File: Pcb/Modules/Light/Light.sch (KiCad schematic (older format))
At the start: 20 parts, among them J1 JACK_RJ45, J2 JACK_STEREO, Q1 TEPT4400, Q2 Q_NMOS_GSD, U1 74LVC1G07, U2 74LVC1G07

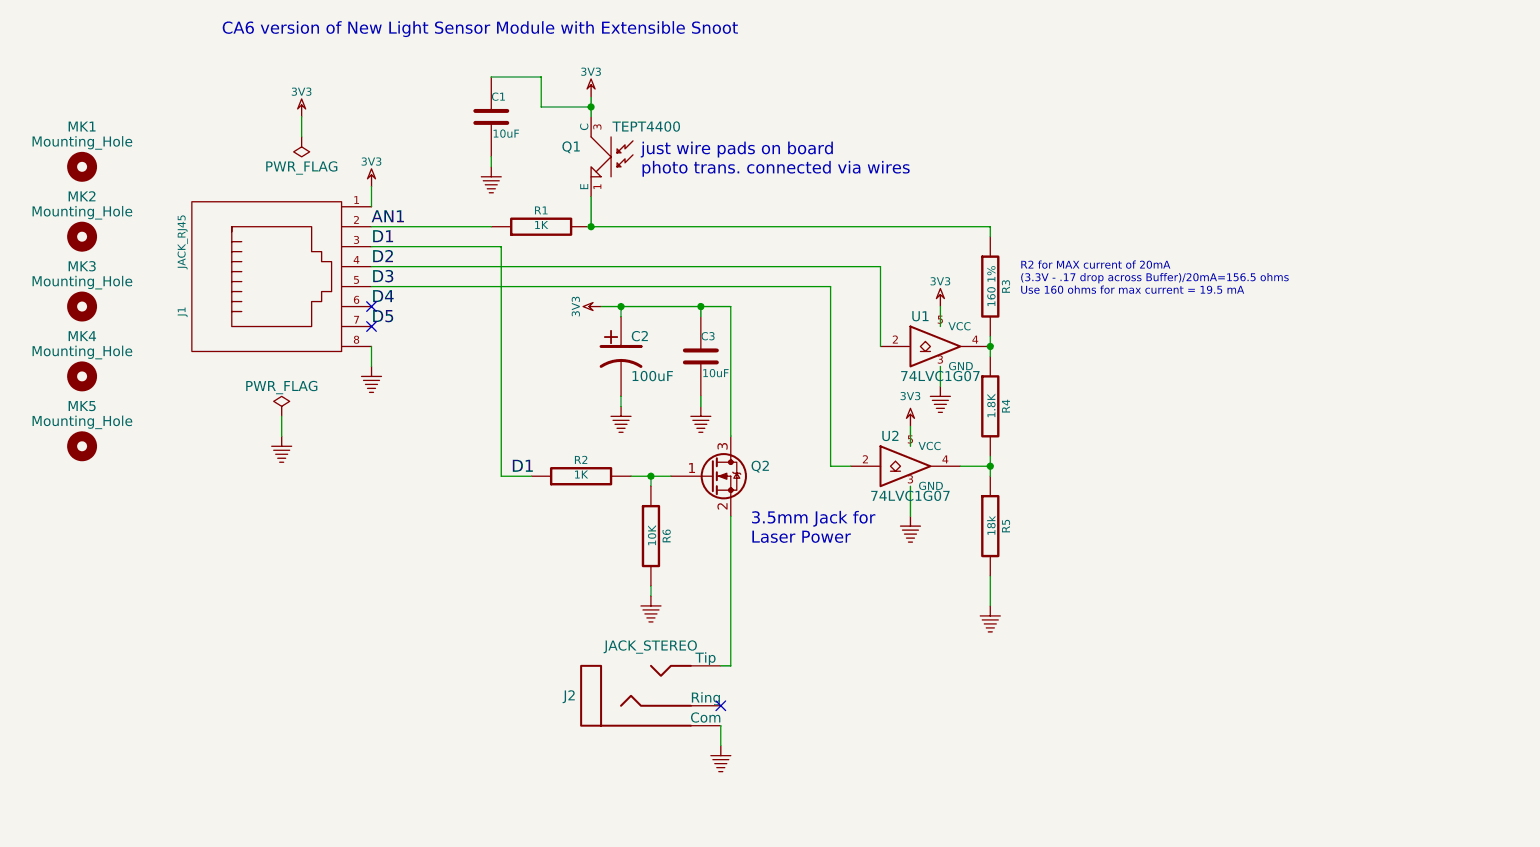
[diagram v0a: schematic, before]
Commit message: Updated schematic for 4-resistor ladder with good values, and moved MOSFET to low (working) position.  PCB only partially updated.  Used a 3rd single buffer for now because I didn't see an exact equivalent in a quad buffer, but that is a likely option.
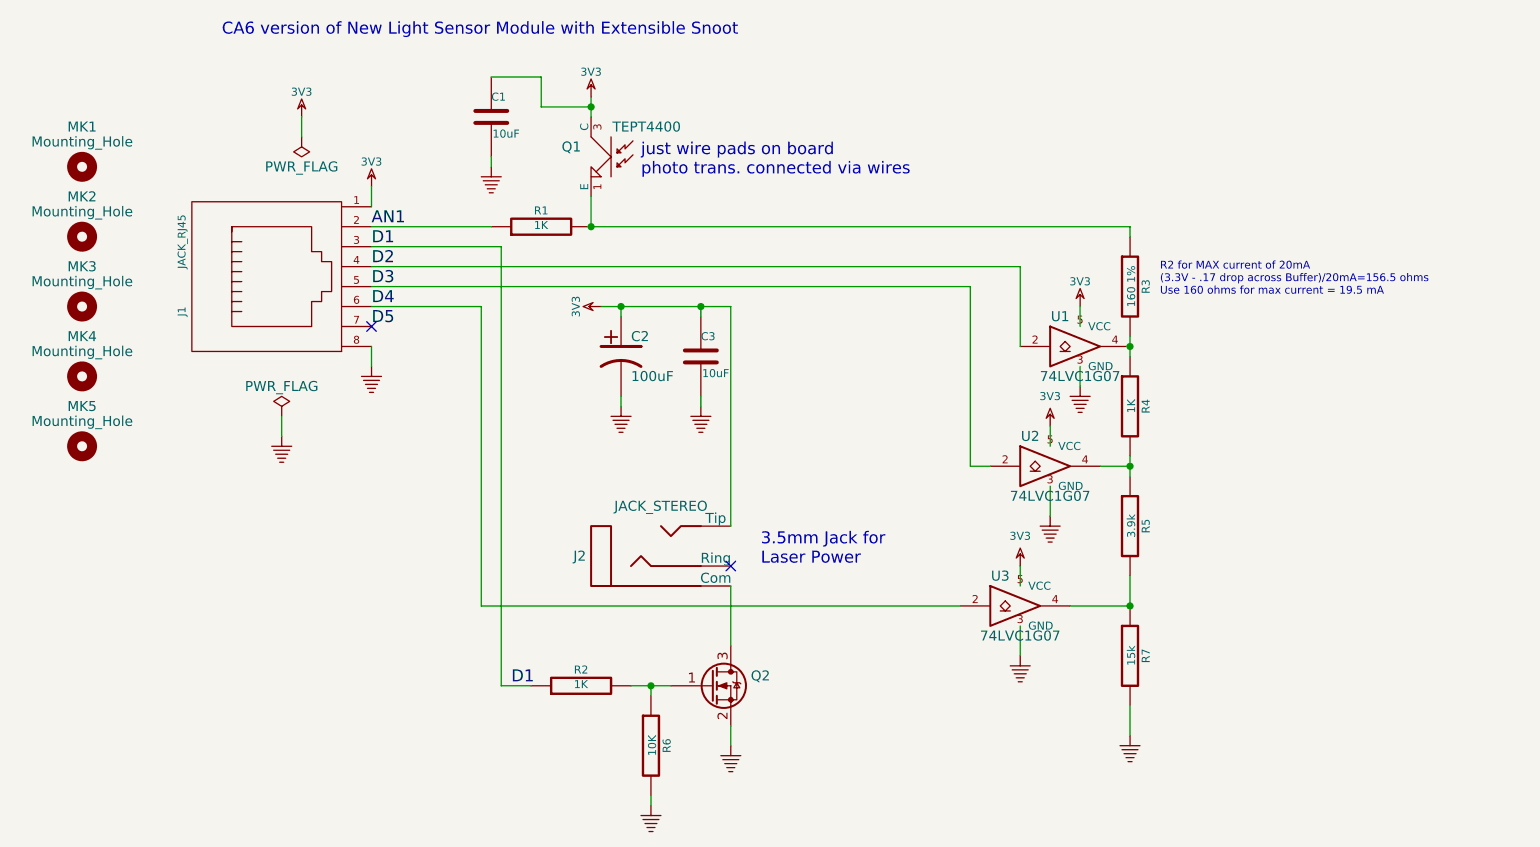
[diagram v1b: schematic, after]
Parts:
- added R7: 15k, CA6:SM0603_Resistor, symbol R
- added U3: 74LVC1G07, TO_SOT_Packages_SMD:SOT-353_SC-70-5, symbol 74LVC1G07
- R4: value 1.8K -> 1K
- R5: value 18k -> 3.9k
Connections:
- net 3V3: now also J2.2 (Tip), U3.5 (VCC); no longer Q2.3 (D)
- net D4: now also U3.2
- net GND: now also Q2.2 (S), R7.2, U3.3 (GND); no longer J2.3 (Com), R5.2
- new net: J2.3 (Com), Q2.3 (D)
- new net: R5.2, R7.1, U3.4
- no-connect marks 3 -> 2
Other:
- moved on the sheet: J2, Q2, R2, R3, R4, R5, R6, U1, U2

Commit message: Updated light module for 3rd buffer and 4 resistors in the ladder, and updated resistor values to give a good change at each step.  Todo: incorporate auto-sensitivity changes into Lightning Menu.
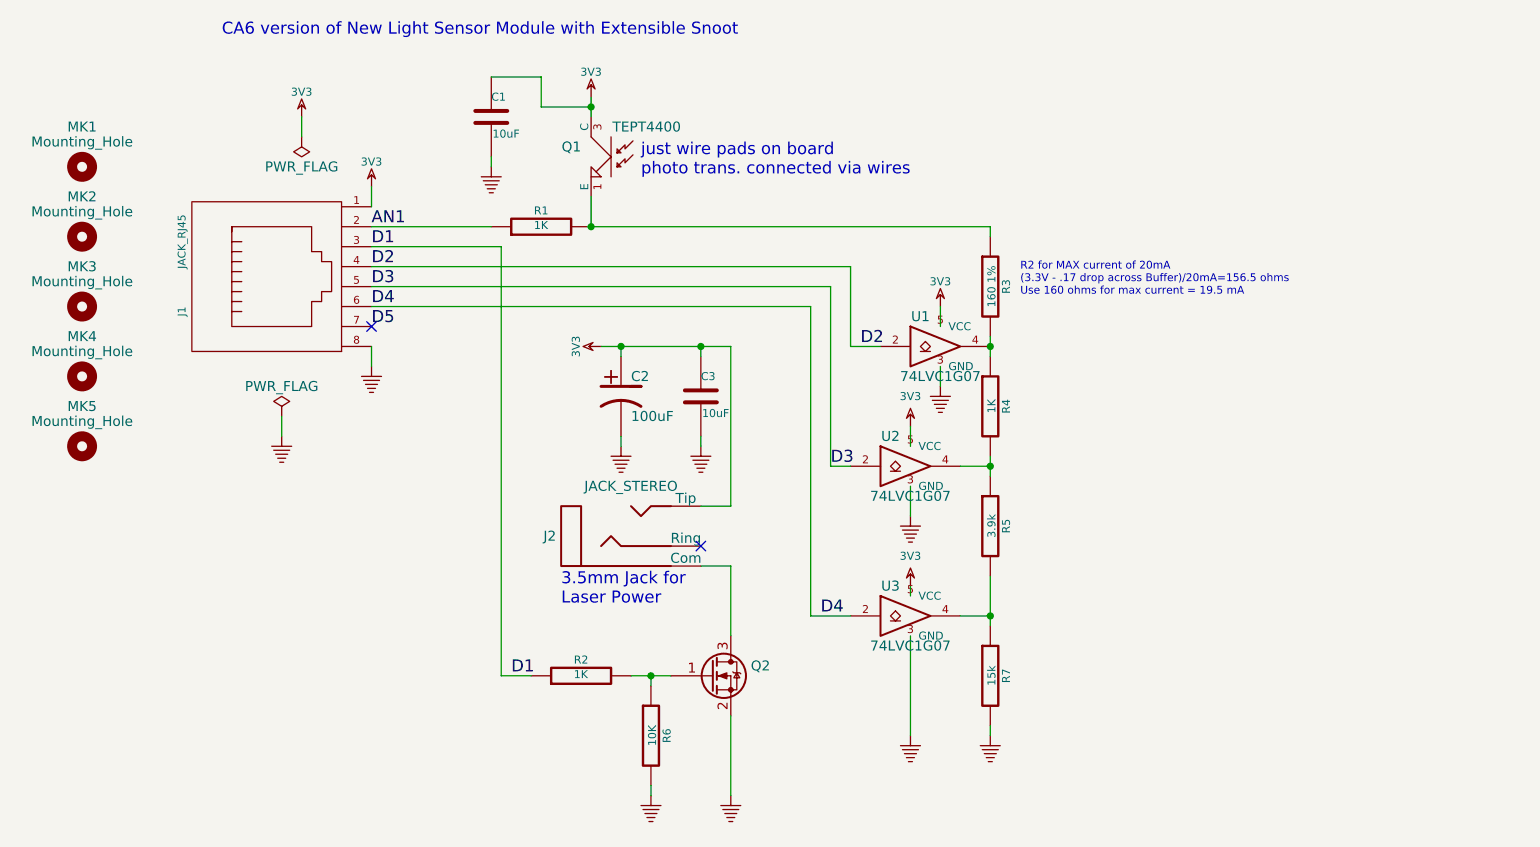
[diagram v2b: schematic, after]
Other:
- moved on the sheet: C2, C3, J2, Q2, R2, R3, R4, R5, R6, U1, U2

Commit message: Update pcb for new switch
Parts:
- C1, C3: symbol C -> CA6:C
- C2: symbol CAP_ELEC -> CA6:CAP_ELEC
- J1: symbol JACK_RJ45 -> CA6:JACK_RJ45
- J2: symbol JACK_STEREO -> CA6:JACK_STEREO
- MK1, MK2, MK3, MK4, MK5: symbol Mounting_Hole -> Light-rescue:Mounting_Hole
- Q1: symbol OPTO_NPN -> CA6:OPTO_NPN
- Q2: symbol Q_NMOS_GSD -> Device:Q_NMOS_GSD
- R1, R2, R3, R4, R5, R6, R7: symbol R -> CA6:R
- U1, U2, U3: symbol 74LVC1G07 -> CA6:74LVC1G07
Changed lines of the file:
@@
-EESchema Schematic File Version 2
-LIBS:CA6
-LIBS:74xx
-LIBS:74xgxx
-LIBS:ac-dc
-LIBS:actel
-LIBS:adc-dac
-LIBS:allegro
-LIBS:Altera
-LIBS:analog_devices
-LIBS:analog_switches
-LIBS:atmel
-LIBS:audio
-LIBS:battery_management
-LIBS:bbd
-LIBS:brooktre
-LIBS:cmos_ieee
-LIBS:cmos4000
-LIBS:conn
-LIBS:contrib
-LIBS:cypress
-LIBS:dc-dc
-LIBS:device
-LIBS:digital-audio
-LIBS:diode
-LIBS:display
-LIBS:dsp
-LIBS:elec-unifil
-LIBS:ESD_Protection
-LIBS:ftdi
-LIBS:gennum
-LIBS:graphic
-LIBS:hc11
-LIBS:intel
-LIBS:interface
-LIBS:ir
-LIBS:Lattice
-LIBS:linear
-LIBS:logo
-LIBS:maxim
-LIBS:mechanical
-LIBS:memory
-LIBS:microchip
-LIBS:microchip_dspic33dsc
-LIBS:microchip_pic10mcu
-LIBS:microchip_pic12mcu
-LIBS:microchip_pic16mcu
-LIBS:microchip_pic18mcu
-LIBS:microchip_pic32mcu
-LIBS:microcontrollers
-LIBS:motor_drivers
-LIBS:motorola
-LIBS:motors
-LIBS:msp430
-LIBS:nordicsemi
-LIBS:nxp_armmcu
-LIBS:onsemi
-LIBS:opto
-LIBS:Oscillators
-LIBS:philips
-LIBS:power
-LIBS:Power_Management
-LIBS:powerint
-LIBS:pspice
-LIBS:references
-LIBS:regul
-LIBS:relays
-LIBS:rfcom
-LIBS:sensors
-LIBS:silabs
-LIBS:siliconi
-LIBS:stm8
-LIBS:stm32
-LIBS:supertex
-LIBS:switches
-LIBS:texas
-LIBS:transf
-LIBS:transistors
-LIBS:ttl_ieee
-LIBS:valves
-LIBS:video
-LIBS:wiznet
-LIBS:Worldsemi
-LIBS:Xicor
-LIBS:xilinx
-LIBS:zetex
-LIBS:Zilog
+EESchema Schematic File Version 4
 LIBS:Light-cache
-EELAYER 25 0
+EELAYER 26 0
 EELAYER END
 $Descr USLetter 11000 8500
@@
 $EndDescr
 $Comp
-L JACK_STEREO J2
+L CA6:JACK_STEREO J2
 U 1 1 54012E4D
 P 5950 4950
@@
 $EndComp
 $Comp
-L JACK_RJ45 J1
+L CA6:JACK_RJ45 J1
 U 1 1 5401301C
 P 4200 3650
@@
 $EndComp
 $Comp
-L 3V3 #PWR01
+L CA6:3V3 #PWR01
 U 1 1 540144B1
 P 4650 3200
@@
 D5
 $Comp
-L GND #PWR02
+L CA6:GND #PWR02
 U 1 1 540144C2
 P 4650 4100
@@
 	4650 3200 4650 3300
 $Comp
-L 3V3 #PWR03
+L CA6:3V3 #PWR03
 U 1 1 5401450D
 P 5800 4000
@@
 D1
 $Comp
-L R R2
+L CA6:R R2
 U 1 1 54AA118B
 P 5700 5650
@@
 $EndComp
 $Comp
-L OPTO_NPN Q1
+L CA6:OPTO_NPN Q1
 U 1 1 54AA12A2
 P 5850 3050
@@
 $EndComp
 $Comp
-L R R1
+L CA6:R R1
 U 1 1 54AA13F6
 P 5500 3400
@@
 $EndComp
 $Comp
-L R R3
+L CA6:R R3
 U 1 1 54AA1792
 P 7750 3700
@@
 $EndComp
 $Comp
-L 3V3 #PWR04
+L CA6:3V3 #PWR04
 U 1 1 54AA199D
 P 5750 2750
@@
 $EndComp
 $Comp
-L GND #PWR05
+L CA6:GND #PWR05
 U 1 1 54AA1A1B
 P 7750 5950
@@
 CA6 version of New Light Sensor Module with Extensible Snoot
 $Comp
-L C C1
+L CA6:C C1
 U 1 1 54AABC31
 P 5250 2850
@@
 $EndComp
 $Comp
-L GND #PWR06
+L CA6:GND #PWR06
 U 1 1 54AABCE0
 P 5250 3100
@@
 NoConn ~ 4650 3900
 $Comp
-L PWR_FLAG #FLG07
+L power:PWR_FLAG #FLG07
 U 1 1 58FEFDE5
 P 4300 2950
@@
 $EndComp
 $Comp
-L 3V3 #PWR08
+L CA6:3V3 #PWR08
 U 1 1 58FEFE63
 P 4300 2850
@@
 	5250 3100 5250 3050
 Wire Wire Line
-	5750 2750 5750 2850
+	5750 2750 5750 2800
 Wire Wire Line
 	5250 2650 5500 2650
@@
 just wire pads on board\nphoto trans. connected via wires
 Wire Wire Line
-	5950 5650 6150 5650
+	5950 5650 6050 5650
 Wire Wire Line
 	5300 5650 5450 5650
@@
 R2 for MAX current of 20mA\n(3.3V - .17 drop across Buffer)/20mA=156.5 ohms\nUse 160 ohms for max current = 19.5 mA
 $Comp
-L PWR_FLAG #FLG09
+L power:PWR_FLAG #FLG09
 U 1 1 59E23186
 P 4200 4350
@@
 $EndComp
 $Comp
-L GND #PWR010
+L CA6:GND #PWR010
 U 1 1 59E231B3
 P 4200 4450
@@
 	4200 4350 4200 4450
 $Comp
-L Q_NMOS_GSD Q2
+L Device:Q_NMOS_GSD Q2
 U 1 1 59E3F4ED
 P 6350 5650
@@
 $EndComp
 $Comp
-L Mounting_Hole MK1
+L Light-rescue:Mounting_Hole MK1
 U 1 1 5A1F1815
 P 3200 3100
@@
 $EndComp
 $Comp
-L Mounting_Hole MK2
+L Light-rescue:Mounting_Hole MK2
 U 1 1 5A1F1870
 P 3200 3450
@@
 $EndComp
 $Comp
-L Mounting_Hole MK3
+L Light-rescue:Mounting_Hole MK3
 U 1 1 5A1F18E3
 P 3200 3800
@@
 $EndComp
 $Comp
-L R R4
+L CA6:R R4
 U 1 1 5A244879
 P 7750 4300
@@
 $EndComp
 $Comp
-L R R5
+L CA6:R R5
 U 1 1 5A2448F7
 P 7750 4900
@@
 Connection ~ 7750 4600
 Wire Wire Line
-	7750 5150 7750 5400
-$Comp
-L 74LVC1G07 U2
+	7750 5150 7750 5350
+$Comp
+L CA6:74LVC1G07 U2
 U 1 1 5A244A16
 P 7350 4600
@@
 $EndComp
 $Comp
-L 74LVC1G07 U1
+L CA6:74LVC1G07 U1
 U 1 1 5A244A65
 P 7500 4000
@@
 	6950 3700 4650 3700
 $Comp
-L GND #PWR011
+L CA6:GND #PWR011
 U 1 1 5A247E92
 P 7350 4850
@@
 $EndComp
 $Comp
-L GND #PWR012
+L CA6:GND #PWR012
 U 1 1 5A247ECA
 P 7500 4200
@@
 $EndComp
 $Comp
-L 3V3 #PWR013
+L CA6:3V3 #PWR013
 U 1 1 5A248403
 P 7500 3800
@@
 $EndComp
 $Comp
-L 3V3 #PWR014
+L CA6:3V3 #PWR014
 U 1 1 5A2484A4
 P 7350 4400
@@
 	6950 4600 7050 4600
 Wire Wire Line
-	7750 4550 7750 4650
-Wire Wire Line
-	7750 3950 7750 4050
+	7750 4550 7750 4600
+Wire Wire Line
+	7750 3950 7750 4000
 Connection ~ 7750 4000
 Wire Wire Line
@@
 	7500 3900 7500 3800
 $Comp
-L C C3
+L CA6:C C3
 U 1 1 5A2877CA
 P 6300 4250
@@
 $EndComp
 $Comp
-L CAP_ELEC C2
+L CA6:CAP_ELEC C2
 U 1 1 5A287922
 P 5900 4250
@@
 $EndComp
 Wire Wire Line
-	5800 4000 6450 4000
+	5800 4000 5900 4000
 Wire Wire Line
 	6450 4000 6450 4800
@@
 Connection ~ 5900 4000
 $Comp
-L GND #PWR015
+L CA6:GND #PWR015
 U 1 1 5A2880E8
 P 5900 4500
@@
 $EndComp
 $Comp
-L GND #PWR016
+L CA6:GND #PWR016
 U 1 1 5A288126
 P 6300 4500
@@
 	5900 4450 5900 4500
 $Comp
-L Mounting_Hole MK4
+L Light-rescue:Mounting_Hole MK4
 U 1 1 5A2EE04A
 P 3200 4150
@@
 $EndComp
 $Comp
-L Mounting_Hole MK5
+L Light-rescue:Mounting_Hole MK5
 U 1 1 5A2EE142
 P 3200 4500
@@
 $EndComp
 $Comp
-L R R6
+L CA6:R R6
 U 1 1 5A32AF14
 P 6050 5950
@@
 Connection ~ 6050 5650
 $Comp
-L GND #PWR017
+L CA6:GND #PWR017
 U 1 1 5A32B0B2
 P 6050 6250
@@
 	6450 5850 6450 6250
 $Comp
-L GND #PWR018
+L CA6:GND #PWR018
 U 1 1 5A36EE99
 P 6450 6250
@@
 $EndComp
 $Comp
-L R R7
+L CA6:R R7
 U 1 1 5A393684
 P 7750 5650
@@
 	7750 5900 7750 5950
 $Comp
-L 74LVC1G07 U3
+L CA6:74LVC1G07 U3
 U 1 1 5A39368C
 P 7350 5350
@@
 $EndComp
 $Comp
-L GND #PWR019
+L CA6:GND #PWR019
 U 1 1 5A393692
 P 7350 5950
@@
 	6850 5350 7050 5350
 $Comp
-L 3V3 #PWR020
+L CA6:3V3 #PWR020
 U 1 1 5A3937A4
 P 7350 5200
@@
 Text Label 6900 5350 0    60   ~ 0
 D4
+Wire Wire Line
+	5750 2800 5750 2850
+Wire Wire Line
+	7750 4600 7750 4650
+Wire Wire Line
+	7750 4000 7750 4050
+Wire Wire Line
+	6300 4000 6450 4000
+Wire Wire Line
+	5900 4000 6300 4000
+Wire Wire Line
+	6050 5650 6150 5650
+Wire Wire Line
+	7750 5350 7750 5400
 $EndSCHEMATC
